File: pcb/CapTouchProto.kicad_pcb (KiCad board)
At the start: 2 copper layers, 73.5 x 64 mm, 44 parts, among them J1 USB_C_Receptacle, J2 62684-50110, Q1 SS8050-G, Q2 SS8050-G, U1 CP2102N-A01-GQFN28, U2 1965-ESP32-WROOM-32E(8MB)CT-ND, U3 AMS1117-3.3

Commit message: Added dot for CP2102N pin 1.
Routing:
- net GND: track 76.3 -> 77.9 mm

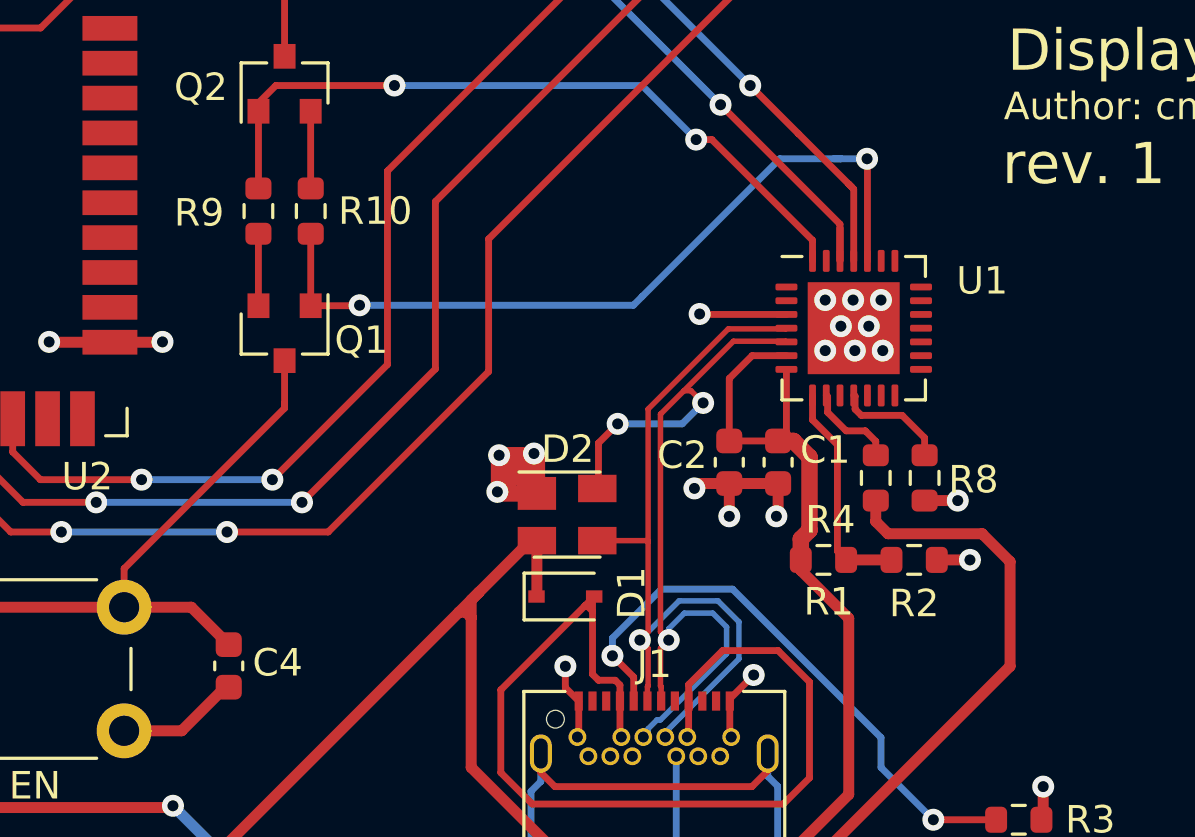
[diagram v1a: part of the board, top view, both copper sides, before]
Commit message: Moved some passives on layout for better labeling.
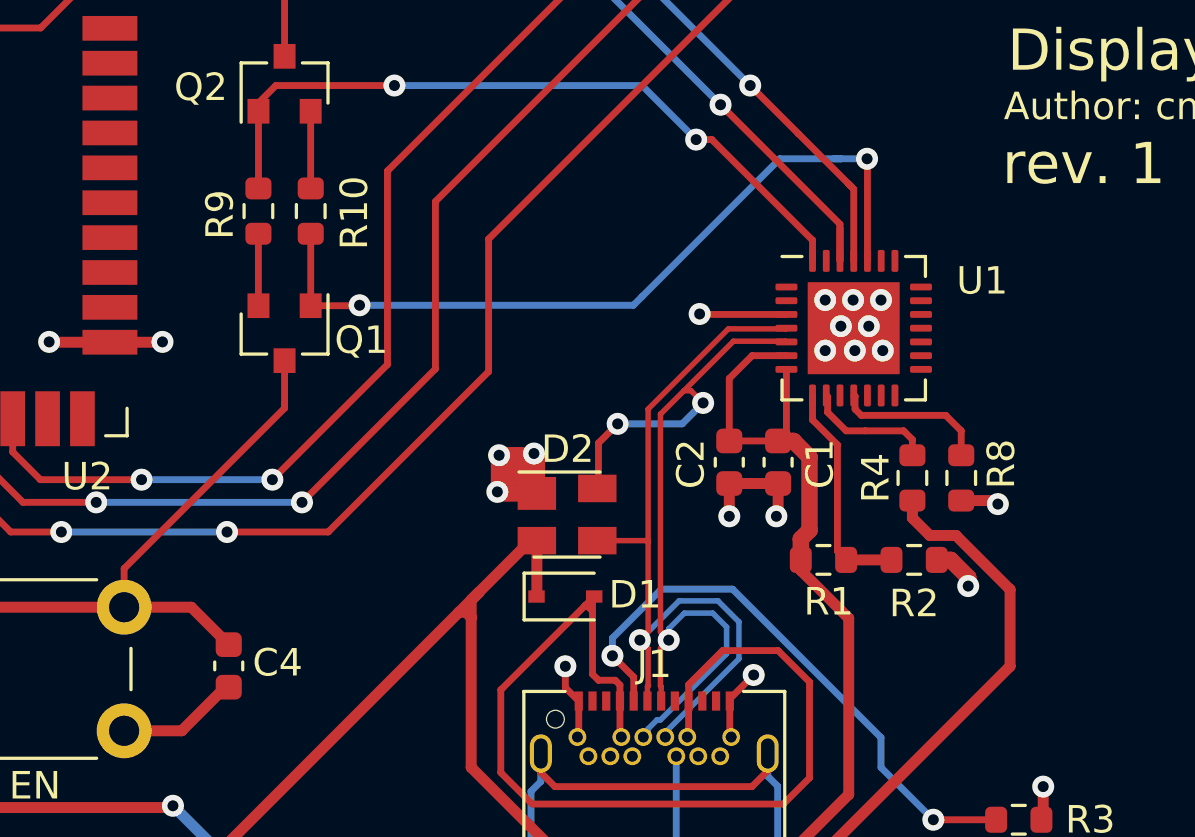
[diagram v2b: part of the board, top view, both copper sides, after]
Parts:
- moved R4 1.33 mm to (182.9, 123.6)
- moved R8 1.33 mm to (184.7, 123.6)
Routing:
- net +3V3: track 233.3 -> 231.7 mm
- net Net-(R8-Pad1): track 4.13 -> 5.61 mm
- net Net-(R4-Pad2): track 3.34 -> 4.71 mm
- net GND: track 77.9 -> 77.3 mm, vias 44 -> 43

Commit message: Testpoint changes.
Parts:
- removed 3V3: 3V3, TestPoint:TestPoint_Pad_D2.5mm
- removed 5V: 5V, TestPoint:TestPoint_Pad_D2.5mm
- removed GND: Conn_01x01_Male, Connector_PinHeader_2.54mm:PinHeader_1x01_P2.54mm_Vertical
- removed the R9 at (159.1, 113.9)
- removed SCL: SCL, TestPoint:TestPoint_Pad_D2.5mm
- removed SDA: SDA, TestPoint:TestPoint_Pad_D2.5mm
- added R17: 10K, Resistor_SMD:R_0603_1608Metric, F.Cu at (159.1, 113.9)
- added TP1: 5V, TestPoint:TestPoint_Pad_D2.5mm, F.Cu at (151.0, 138.4)
- added TP2: SCL, TestPoint:TestPoint_Loop_D2.50mm_Drill1.0mm, F.Cu at (141.6, 89.2)
- added TP3: SDA, TestPoint:TestPoint_Loop_D2.50mm_Drill1.0mm, F.Cu at (149.6, 89.4)
- added TP4: GND, TestPoint:TestPoint_Loop_D2.50mm_Drill1.0mm, F.Cu at (157.4, 93.3)
- added TP5: 3V3, TestPoint:TestPoint_Pad_D2.5mm, F.Cu at (146.3, 138.4)
- renumbered BOOT to BOOT1, C3 to C1, C6 to C2, C7 to C3, C1 to C6, C2 to C7, EN to EN1, R15 to R1, R4 to R10, R1 to R11, R6 to R12, R7 to R13, R2 to R14, R12 to R15, R8 to R16, R10 to R18, R16 to R2, R17 to R3, R18 to R4, R3 to R5, R5 to R6, R11 to R7, R13 to R8, R14 to R9, U2 to U1, U3 to U2, U1 to U3
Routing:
- net Net-(J2-Pad45): track 80.8 -> 77.9 mm
- net Net-(J2-Pad44): track 102.8 -> 101.1 mm
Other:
- board text added: "rev. 2"
- board text removed: "rev. 1"

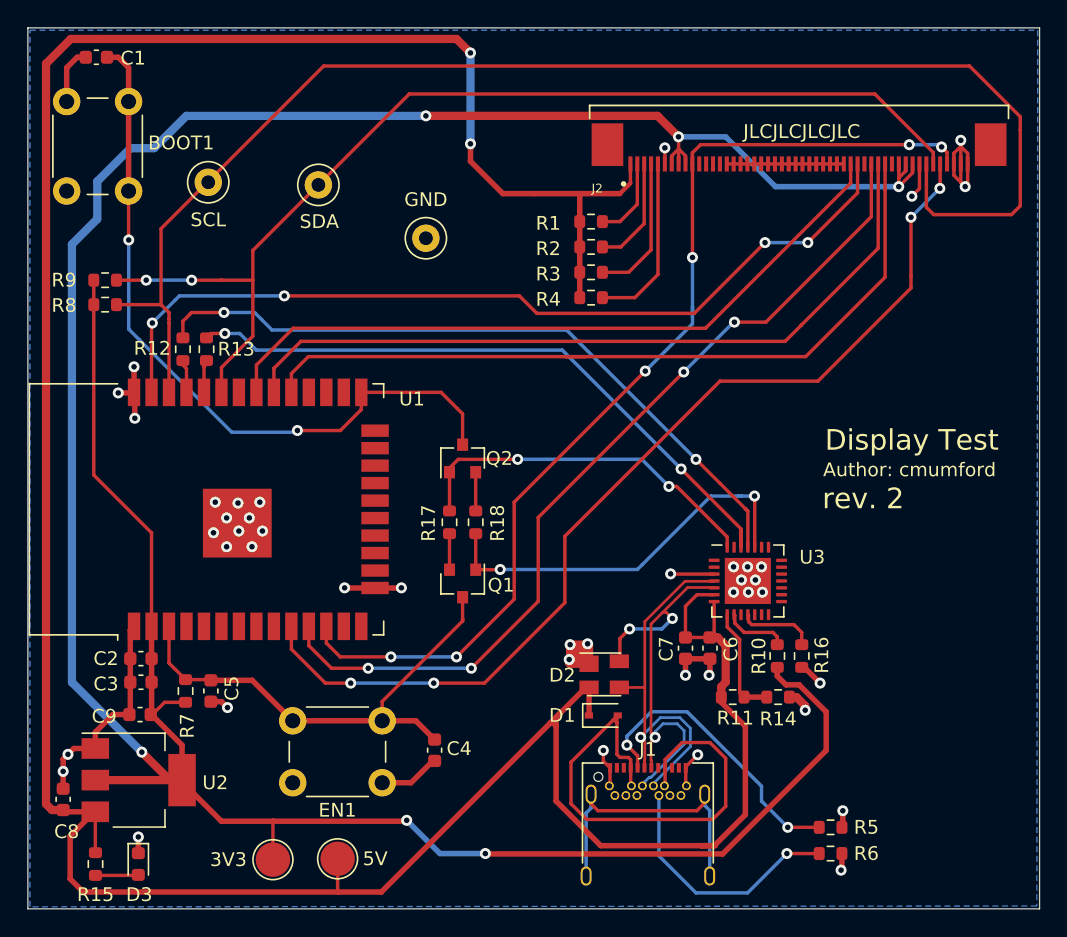
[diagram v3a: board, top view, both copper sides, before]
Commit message: Fix switch labeling, more cleanup.
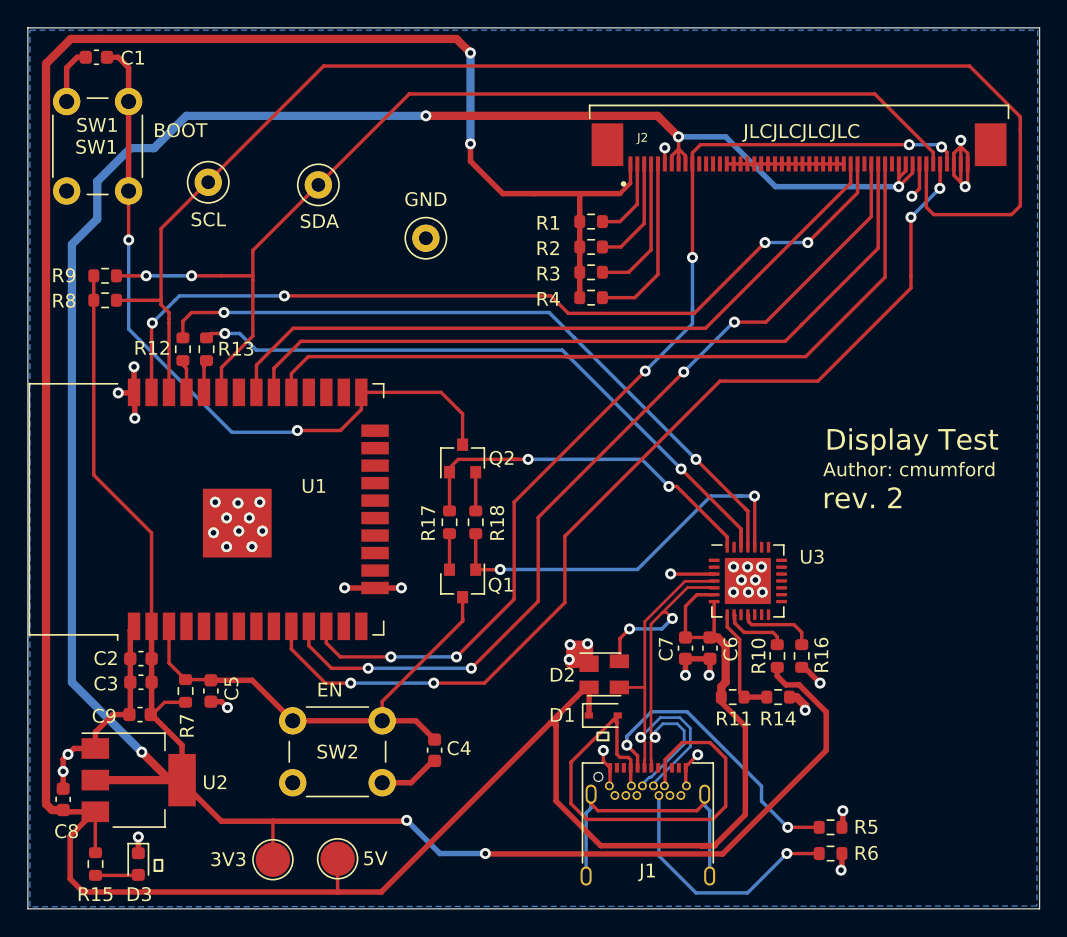
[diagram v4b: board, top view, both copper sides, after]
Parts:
- removed EN1: SW_Push, Button_Switch_THT:SW_PUSH_6mm_H5mm
- added SW2: EN, Button_Switch_THT:SW_PUSH_6mm_H5mm, F.Cu at (154.2, 132.8)
- SW1: renamed from BOOT1; value SW_Push -> BOOT
- moved R8 0.32 mm to (134.1, 97.8)
- moved R9 0.32 mm to (134.1, 96.0)
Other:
- board text added: "⏄"

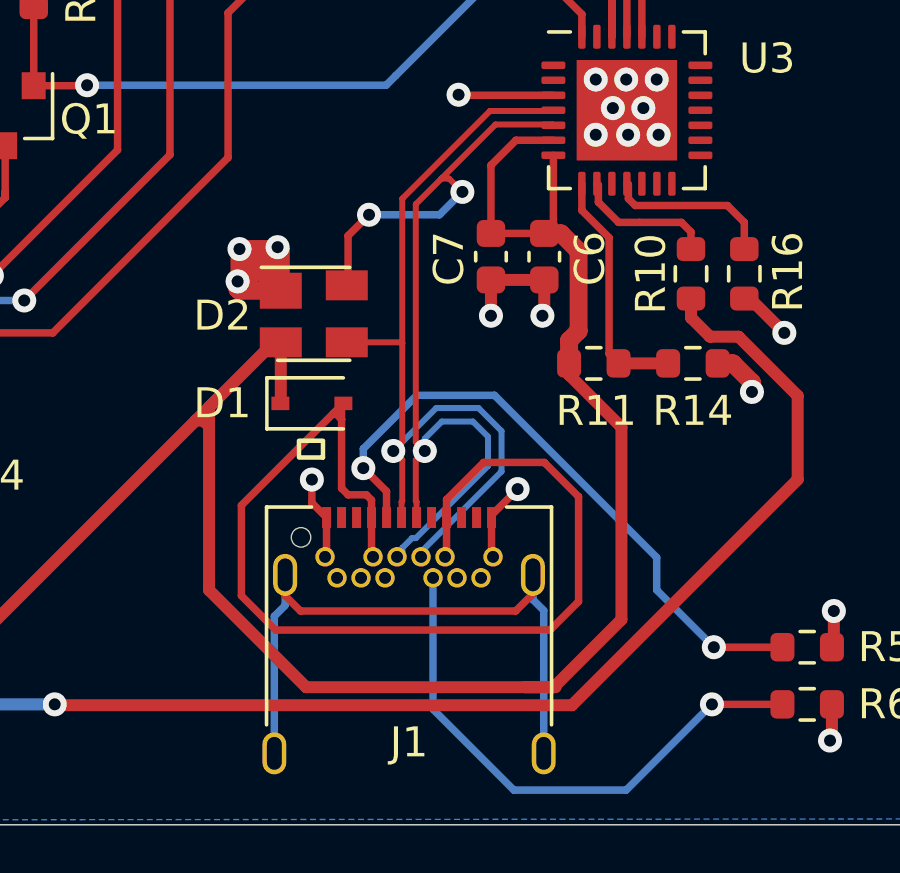
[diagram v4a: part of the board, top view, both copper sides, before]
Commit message: CP2102 VCC/REGIN pins to 3.3V instead of VBUS.
Oops!
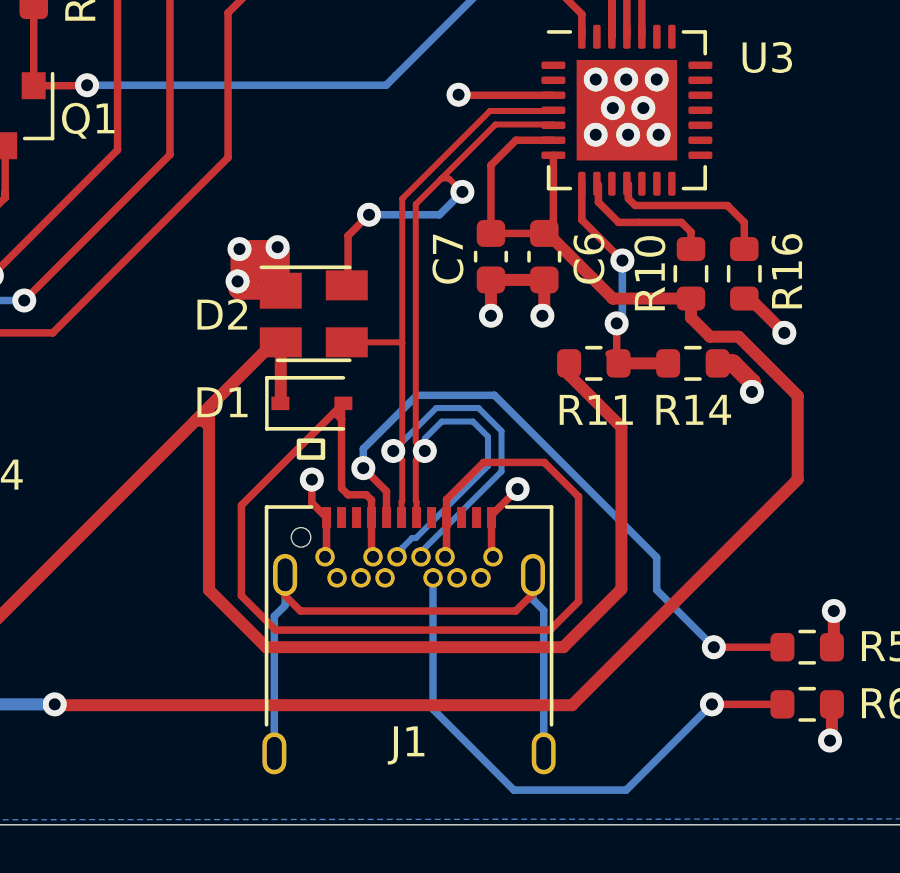
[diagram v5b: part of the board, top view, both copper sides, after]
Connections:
- C6 pad 1: VBUS -> +3V3
- C7 pad 1: VBUS -> +3V3
- U3 pad 6: VBUS -> +3V3
- U3 pad 7: VBUS -> +3V3
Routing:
- net VBUS: track 224.6 -> 207.4 mm
- net +3V3: track 231.7 -> 246.8 mm
- net Net-(R11-Pad2): track 8.15 -> 8.75 mm, vias 0 -> 2
